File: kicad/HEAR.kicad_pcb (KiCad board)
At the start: 2 copper layers, 39.3 x 106.5 mm, 56 parts, among them J1 PJ341, J12 Euro power header, J13 PJ341, J14 PJ341, J2 PJ341, J3 PJ341, J4 PJ341, J5 Attenuator Jumper 1, J6 Attenuator Jumper 2, U1 TL074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

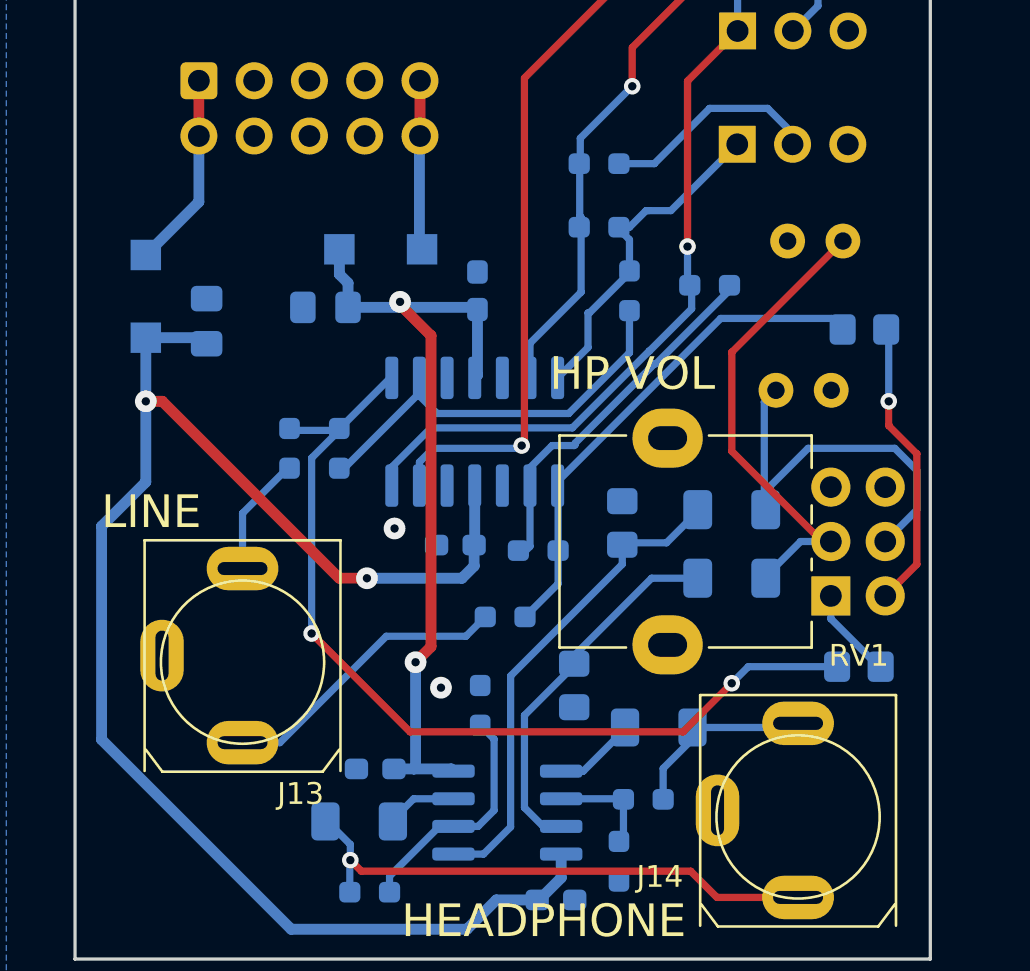
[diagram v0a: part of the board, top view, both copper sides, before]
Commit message: updated diode footprint for new jlcpart
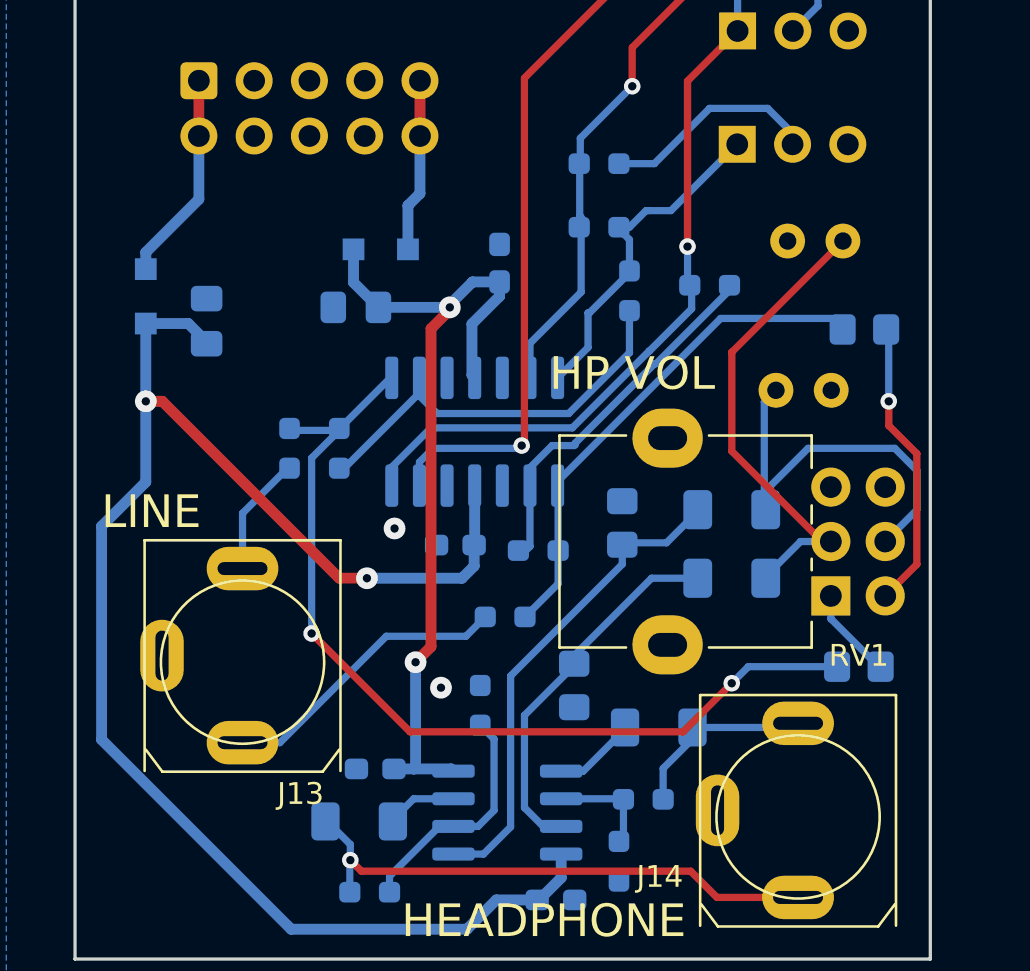
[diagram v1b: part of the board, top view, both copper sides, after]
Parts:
- D1, D2: footprint nearness:SOD-123 -> Diode_SMD:D_SOD-323_HandSoldering
- moved C7 1.63 mm to (33.8, 100.1)
- moved C5 1.40 mm to (27.2, 102.1)
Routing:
- net +12V: track 37.5 -> 39.0 mm
- net -12V: track 71.4 -> 72.3 mm
- net Net-(D2-Pad1): track 9.02 -> 9.67 mm
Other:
- rule pad_to_mask_clearance: 0.1016 -> 0

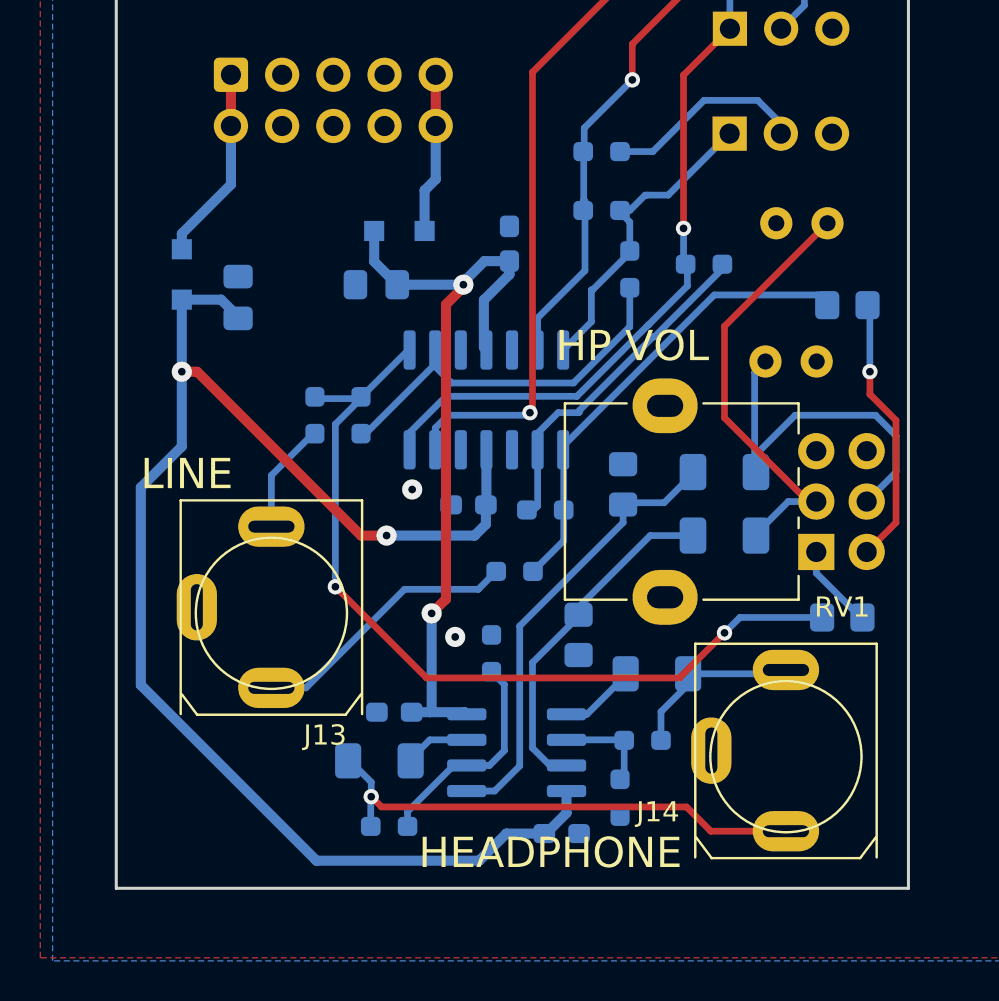
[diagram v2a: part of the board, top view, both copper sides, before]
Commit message: re-route for better symmetry
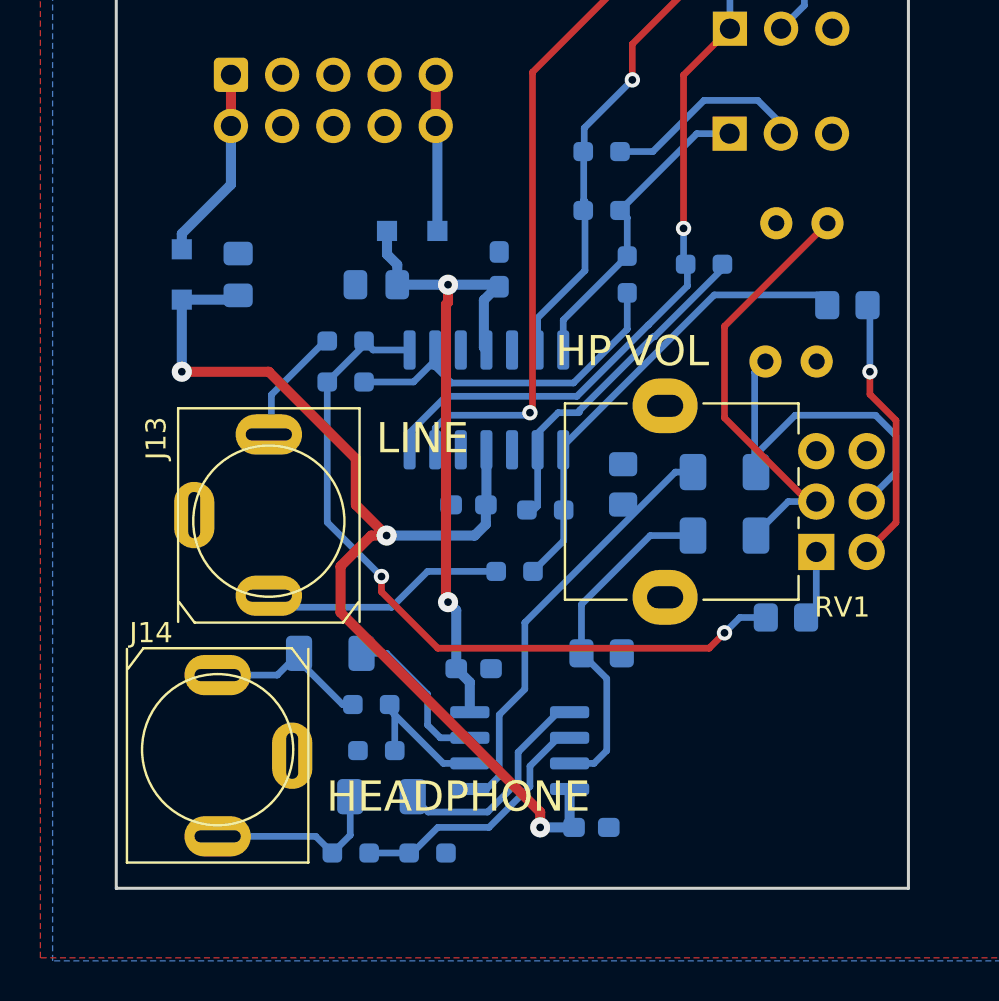
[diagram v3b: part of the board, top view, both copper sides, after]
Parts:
- moved J14 28.2 mm to (19.3, 125.5), turned to 0 degrees
- moved R25 15.5 mm to (25.9, 130.3), turned to 0 degrees
- moved R33 15.0 mm to (27.4, 127.5), turned to 0 degrees
- moved R23 9.94 mm to (29.7, 130.3), turned to 180 degrees
- moved R24 7.48 mm to (27.2, 125.2), turned to 0 degrees
- moved R26 6.11 mm to (26.9, 122.9)
- moved R34 5.86 mm to (24.9, 120.4)
- moved J13 4.57 mm to (21.8, 113.5)
- moved C9 4.49 mm to (32.0, 121.2), turned to 0 degrees
- moved R29 3.99 mm to (25.7, 104.9), turned to 180 degrees
- moved R35 2.79 mm to (47.5, 118.6)
- moved R27 1.82 mm to (25.7, 106.9), turned to 180 degrees
- moved C10 1.50 mm to (37.8, 129.0)
- moved R15 1.46 mm to (38.4, 120.4), turned to 180 degrees
- moved C7 1.37 mm to (33.3, 101.3)
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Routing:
- net -12V: track 72.3 -> 53.8 mm, vias 2 -> 3
- net HPoutR: track 25.0 -> 8.43 mm, vias 1 -> 0
- net Net-(R23-Pad2): track 4.89 -> 12.9 mm
- net Net-(R33-Pad2): track 3.85 -> 11.0 mm
- net +12V: track 39.0 -> 33.3 mm
- net Lout: track 43.0 -> 37.6 mm
- net Net-(R34-Pad2): track 3.30 -> 8.00 mm
- net Net-(R24-Pad2): track 11.0 -> 7.73 mm
- net Net-(R21-Pad2): track 19.8 -> 18.1 mm
- net RLineOut: track 13.5 -> 12.3 mm
- net Net-(C2-Pad2): track 22.5 -> 21.4 mm
- net Net-(R35-Pad1): track 4.16 -> 3.46 mm
- net GND: vias 2 -> 0
